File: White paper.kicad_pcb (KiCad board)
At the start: 4 copper layers, 100 x 100 mm, 35 parts, among them J1 Conn_Coaxial, J10 Conn_Coaxial, J11 Conn_Coaxial, J12 Conn_Coaxial, J13 Conn_Coaxial, J14 Conn_Coaxial, J15 Conn_Coaxial, J16 Conn_Coaxial, J2 Conn_Coaxial, J3 Conn_Coaxial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

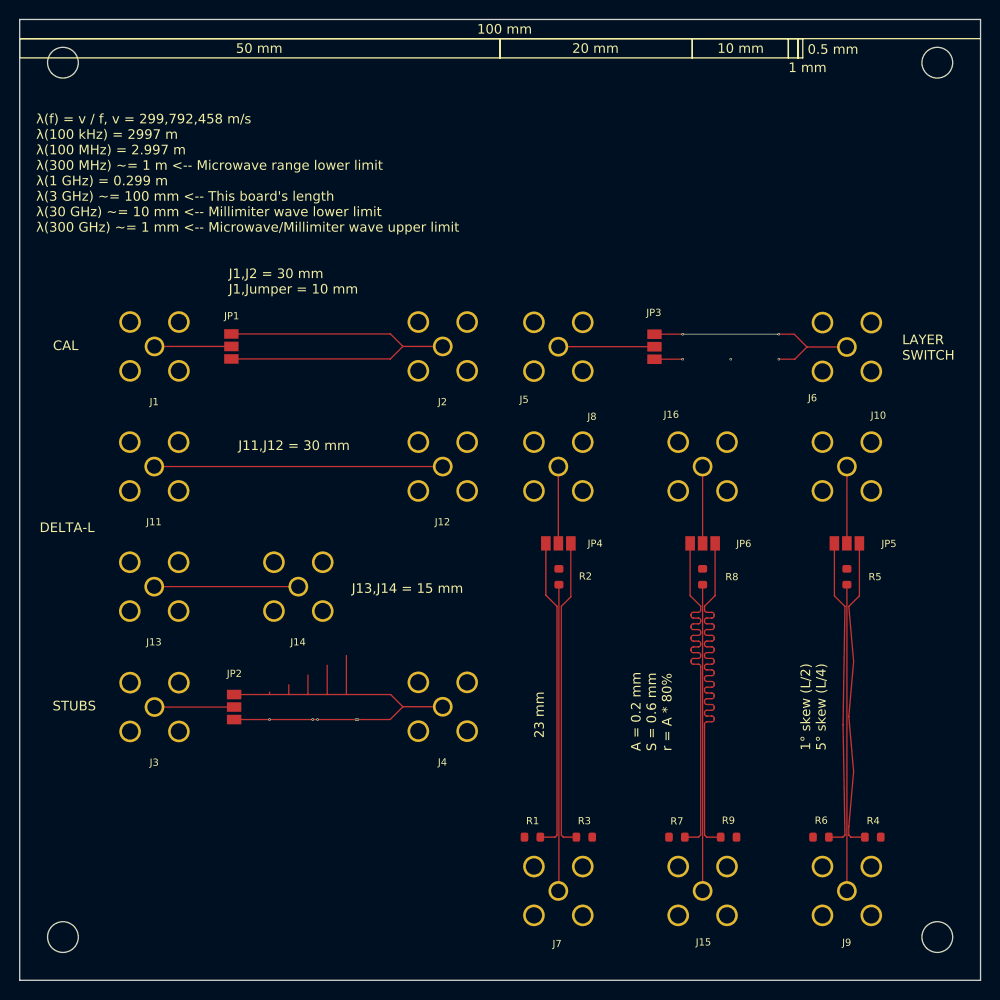
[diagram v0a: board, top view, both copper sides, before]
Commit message: Rev B
Added 50R controlled Z, SOLT calibration and more reasonable tests
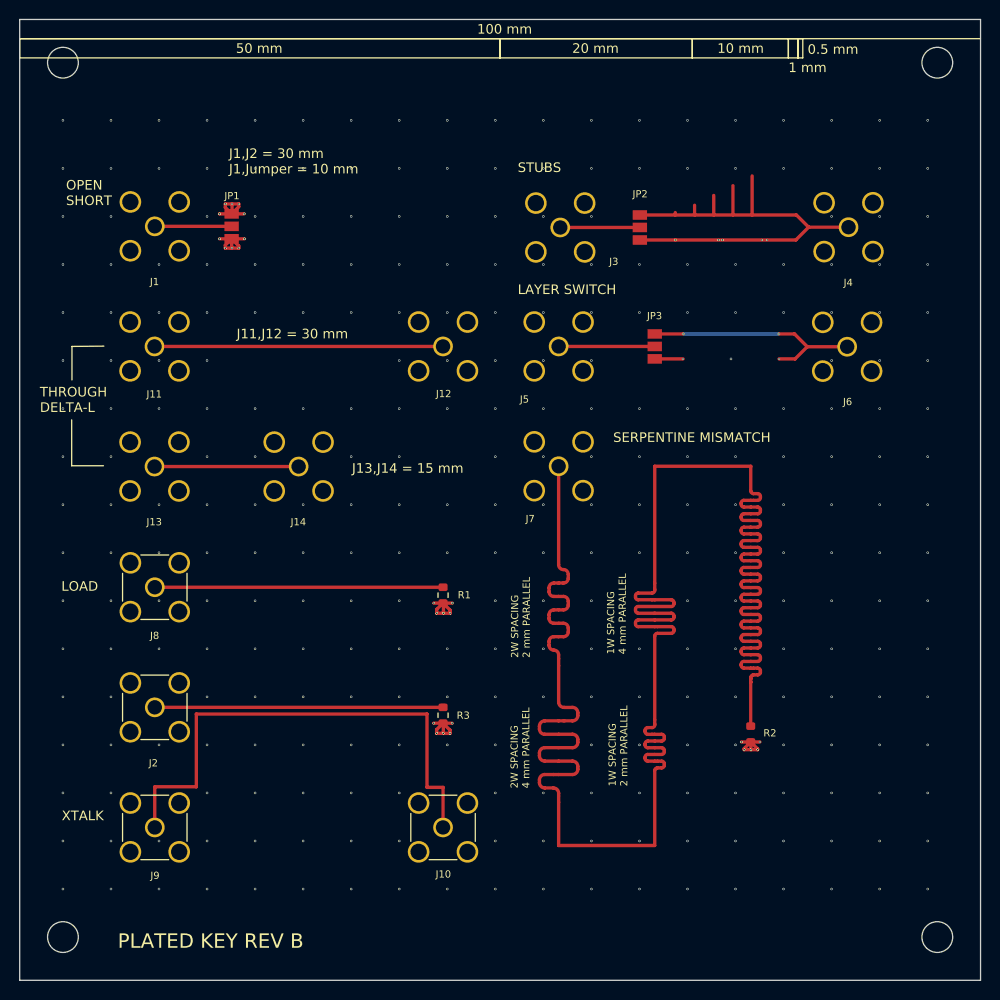
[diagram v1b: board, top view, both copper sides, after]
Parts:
- removed J15, J16: Conn_Coaxial, Library:SMA
- removed JP4, JP5, JP6: SolderJumper_3_Open, Jumper:SolderJumper-3_P1.3mm_Open_Pad1.0x1.5mm
- removed R4, R5, R6, R7, R8, R9: 50R, Resistor_SMD:R_0603_1608Metric
- moved J9 72.3 mm to (64.0, 134.1)
- moved J3 65.4 mm to (106.2, 71.6)
- moved JP2 65.4 mm to (114.5, 71.7)
- moved J4 65.4 mm to (136.2, 71.6)
- moved J10 56.4 mm to (94.0, 134.1)
- moved J2 48.1 mm to (64.0, 121.6)
- moved J7 44.2 mm to (106.1, 96.5)
- moved J8 43.9 mm to (64.0, 109.1), turned to 0 degrees
- moved R1 26.8 mm to (94.1, 109.9), turned to -90 degrees
- moved R2 25.8 mm to (126.1, 124.4), turned to -90 degrees
- moved R3 19.4 mm to (94.1, 122.4), turned to -90 degrees
- moved J1 12.5 mm to (64.0, 71.5)
- moved J11 12.5 mm to (64.0, 84.0)
- moved J12 12.5 mm to (94.0, 84.0)
- moved J13 12.5 mm to (64.0, 96.5)
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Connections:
- J9 pad 1: Net-(J9-In) -> Net-(J10-In)
- JP1 pad 1: Net-(J2-In) -> GND
- JP1 pad 3: Net-(J2-In) -> GND
- R1 pad 1: Net-(JP4-B) -> Net-(J8-In)
- R3 pad 1: Net-(JP4-A) -> Net-(J2-In)
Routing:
- net Net-(J7-In): track 31.9 -> 234.0 mm
- net Net-(JP6-A): track 48.1 -> 0.00 mm
- net Net-(J10-In): track 8.00 -> 53.6 mm
- net Net-(JP6-B): track 40.3 -> 0.00 mm
- net GND: track 0.00 -> 35.7 mm, vias 0 -> 326
- net Net-(JP4-B): track 32.7 -> 0.00 mm
- net Net-(JP5-A): track 32.7 -> 0.00 mm
- net Net-(JP5-B): track 32.6 -> 0.00 mm
- net Net-(JP4-A): track 32.4 -> 0.00 mm
- net Net-(J9-In): track 31.9 -> 0.00 mm
- net Net-(J15-In): track 31.9 -> 0.00 mm
- net Net-(J8-In): track 8.00 -> 30.0 mm
- net Net-(J2-In): track 40.9 -> 30.0 mm
- net Net-(J16-In): track 8.00 -> 0.00 mm
- added copper zone on In1.Cu, net GND
- added copper zone on In2.Cu, net GND
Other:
- board text added: "0"
- board text added: "0 mm"
- board text added: "0.01 mm"
- board text added: "0.0152 mm"
- board text added: "0.02"
- board text added: "0.035 mm"
- board text added: "0.1000 mm / 0.1000 mm"
- board text added: "0.2"
- board text added: "0.2104 mm"
- board text added: "0.2500 mm"
- board text added: "1"
- board text added: "1.065 mm"
- board text added: "1.6062 mm"
- board text added: "100.0000 mm x 100.0000 mm"
- board text added: "1W SPACING 2 mm PARALLEL"
- board text added: "1W SPACING 4 mm PARALLEL"
- board text added: "2W SPACING 2 mm PARALLEL"
- board text added: "2W SPACING 4 mm PARALLEL"
- board text added: "3.8"
- board text added: "4"
- board text added: "4.5"
- board text added: "4.6"
- board text added: "B.Cu"
- board text added: "B.Mask"
- board text added: "B.Paste"
- board text added: "B.Silkscreen"
- board text added: "BOARD CHARACTERISTICS"
- board text added: "Board Thickness:"
- board text added: "Board overall dimensions:"
- board text added: "Bottom Silk Screen"
- board text added: "Bottom Solder Mask"
- board text added: "Bottom Solder Paste"
- board text added: "Castellated pads:"
- board text added: "Color"
- board text added: "Copper Finish:"
- board text added: "Copper Layer Count:"
- board text added: "Dielectric 1"
- board text added: "Dielectric 2"
- board text added: "Dielectric 3"
- board text added: "Edge card connectors:"
- board text added: "Epsilon R"
- board text added: "F.Cu"
- board text added: "F.Mask"
- board text added: "F.Paste"
- board text added: "F.Silkscreen"
- board text added: "FR4"
- board text added: "FR4 natural"
- board text added: "Green"
- board text added: "HASL"
- board text added: "Impedance Control:"
- board text added: "Impedance targets: 50 Ohm (L1, L2, L3, L4)"
- board text added: "In1.Cu"
- board text added: "In2.Cu"
- board text added: "LOAD"
- board text added: "Layer Name"
- board text added: "Loss Tangent"
- board text added: "Material"
- board text added: "Min hole diameter:"
- board text added: "Min track/spacing:"
- board text added: "No"
- board text added: "Not specified"
- board text added: "OPEN SHORT"
- board text added: "PLATED KEY REV B"
- board text added: "Plated Board Edge:"
- board text added: "SERPENTINE MISMATCH"
- board text added: "THROUGH DELTA-L"
- board text added: "Thickness (mm)"
- board text added: "Top Silk Screen"
- board text added: "Top Solder Mask"
- board text added: "Top Solder Paste"
- board text added: "Type"
- board text added: "White"
- board text added: "XTALK"
- board text added: "Yes"
- board text added: "copper"
- board text added: "core"
- board text added: "prepreg"
- board text removed: "1° skew (L/2) 5° skew (L/4)"
- board text removed: "23 mm"
- board text removed: "A = 0.2 mm S = 0.6 mm r = A * 80%"
- board text removed: "CAL"
- board text removed: "DELTA-L"
